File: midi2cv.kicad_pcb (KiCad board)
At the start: 2 copper layers, 20.2 x 123.5 mm, 23 parts, among them J1 AudioJack3, J2 Conn_02x05_Top_Bottom, J3 AudioJack2_SwitchT, J4 AudioJack2_SwitchT, J5 AudioJack2_SwitchT, J6 AudioJack2_SwitchT, J7 AudioJack3, Q1 BC548, U1 6N138

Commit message: routed pcb
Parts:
- removed Q1: BC548, Package_TO_SOT_THT:TO-92_Inline_Wide
- added B2: Board, Custom:Board_4hp_100mm, F.Cu at (127.0, 95.2)
- added B3: Front_Plate, Custom:Front_Plate_4hp_cut, F.Cu at (190.5, 95.2)
- added C10: 1n, Capacitor_SMD:C_0603_1608Metric, F.Cu at (121.5, 141.5)
- added C11: 1n, Capacitor_SMD:C_0603_1608Metric, F.Cu at (135.3, 141.5)
- added C12: 1n, Capacitor_SMD:C_0603_1608Metric, F.Cu at (132.3, 141.0)
- added C13: 1n, Capacitor_SMD:C_0603_1608Metric, F.Cu at (121.5, 121.0)
- added C14: 1n, Capacitor_SMD:C_0603_1608Metric, F.Cu at (123.1, 116.0)
- added C17: 10n, Capacitor_SMD:C_0603_1608Metric, F.Cu at (128.8, 123.4)
- added C7: 1n, Capacitor_SMD:C_0603_1608Metric, F.Cu at (118.9, 140.7)
- added C8: 100n, Capacitor_SMD:C_0603_1608Metric, F.Cu at (128.8, 135.6)
- added C9: 100n, Capacitor_SMD:C_0603_1608Metric, F.Cu at (125.1, 142.7)
- added D2: 1N5819WS, Diode_SMD:D_SOD-323, F.Cu at (120.1, 78.7)
- added D3: 1N5819WS, Diode_SMD:D_SOD-323, F.Cu at (131.8, 78.7)
- added D5: LED, LED_THT:LED_D3.0mm, B.Cu at (121.9, 94.0)
- added D6: LED, LED_THT:LED_D3.0mm, B.Cu at (129.5, 94.0)
- added H1: 6mm, Custom:DrillHole_D6.00, F.Cu at (185.4, 52.1)
- added H10: 7mm, Custom:DrillHole_D7.00, F.Cu at (190.5, 112.4)
- added H2: 6mm, Custom:DrillHole_D6.00, F.Cu at (185.4, 63.5)
- added H3: 6mm, Custom:DrillHole_D6.00, F.Cu at (190.5, 126.4)
- added H4: 6mm, Custom:DrillHole_D6.00, F.Cu at (185.4, 138.4)
- added H5: 6mm, Custom:DrillHole_D6.00, F.Cu at (195.6, 52.1)
- added H6: 6mm, Custom:DrillHole_D6.00, F.Cu at (195.6, 63.5)
- added H7: 6mm, Custom:DrillHole_D6.00, F.Cu at (195.6, 138.4)
- added H8: 3mm, Custom:DrillHole_D3.00, F.Cu at (186.7, 94.0)
- added H9: 3mm, Custom:DrillHole_D3.00, F.Cu at (194.3, 94.0)
- added J8: CC, Custom:Jack_3.5mm_QingPu_WQP-PJ398SM_Vertical_CircularHoles_L, B.Cu at (127.0, 126.4)
- added J9: Conn_02x04_Odd_Even, Connector_PinSocket_1.27mm:PinSocket_2x04_P1.27mm_Vertical, F.Cu at (119.4, 131.4)
- added JP1: Jumper_3_Bridged12, Connector_PinHeader_2.54mm:PinHeader_1x03_P2.54mm_Vertical, F.Cu at (134.6, 126.9)
- added R10: 1k, Resistor_SMD:R_0603_1608Metric, F.Cu at (129.3, 143.3)
- added R11: 1k, Resistor_SMD:R_0603_1608Metric, F.Cu at (132.1, 97.2)
- added R12: 15k, Resistor_SMD:R_0603_1608Metric, F.Cu at (118.9, 137.4)
- added R13: 15k, Resistor_SMD:R_0603_1608Metric, F.Cu at (121.5, 140.0)
- added R14: 15k, Resistor_SMD:R_0603_1608Metric, F.Cu at (135.3, 138.4)
- added R15: 15k, Resistor_SMD:R_0603_1608Metric, F.Cu at (132.3, 139.3)
- added R16: 15k, Resistor_SMD:R_0603_1608Metric, F.Cu at (121.5, 116.0)
- added R17: 15k, Resistor_SMD:R_0603_1608Metric, F.Cu at (122.3, 118.2)
- added R18: 100, Resistor_SMD:R_0603_1608Metric, F.Cu at (131.4, 120.7)
- added R23: 1k, Resistor_SMD:R_0603_1608Metric, F.Cu at (125.5, 123.4)
- added R24: 1k, Resistor_SMD:R_0603_1608Metric, F.Cu at (119.8, 67.3)
- added R25: 100k, Resistor_SMD:R_0603_1608Metric, F.Cu at (130.8, 130.3)
- added R27: 1k, Resistor_SMD:R_0603_1608Metric, F.Cu at (128.9, 96.5)
- added R7: 1k, Resistor_SMD:R_0603_1608Metric, F.Cu at (122.4, 137.7)
- added R8: 1k, Resistor_SMD:R_0603_1608Metric, F.Cu at (124.9, 67.3)
- added R9: 1k, Resistor_SMD:R_0603_1608Metric, F.Cu at (127.6, 67.3)
- added RV1: 20k, Potentiometer_THT:Potentiometer_Vishay_T93XA_Horizontal, B.Cu at (124.5, 104.8)
- added RV2: 100k, Potentiometer_THT:Potentiometer_Vishay_T93XA_Horizontal, B.Cu at (124.5, 99.1)
- added RV5: A100k, EuroRackTools:Potentiometer_Alpha_RD901F-40-00D_Single_Vertical, B.Cu at (129.5, 120.0)
- added U3: TL072, Package_SO:SOIC-8_3.9x4.9mm_P1.27mm, F.Cu at (127.0, 139.2)
- added U4: TL072, Package_SO:SOIC-8_3.9x4.9mm_P1.27mm, F.Cu at (127.0, 108.6)
- C1: footprint Capacitor_THT:C_Disc_D3.0mm_W2.0mm_P2.50mm -> Capacitor_SMD:C_0603_1608Metric
- C2, C3: value 100p -> 100n; footprint Capacitor_THT:C_Disc_D3.0mm_W2.0mm_P2.50mm -> Capacitor_SMD:C_0603_1608Metric
- C4, C5, C6: footprint Capacitor_THT:CP_Radial_D5.0mm_P2.00mm -> Capacitor_SMD:C_0805_2012Metric
- D1: value 1N4148 -> 1N4148WS; footprint Diode_THT:D_DO-35_SOD27_P2.54mm_Vertical_AnodeUp -> Diode_SMD:D_SOD-323
- J1: value AudioJack3 -> MIDI In; footprint TRS_AudioConn3:Jack_3.5mm_QingPu_WQP-PJ366ST_Vertical -> Custom:Jack_3.5mm_QingPu_WQP-PJ366ST_Vertical_CircularHoles_L; moved to B.Cu
- J2: value Conn_02x05_Top_Bottom -> EuroPower10_THT; footprint Connector_IDC:IDC-Header_2x05_P2.54mm_Vertical -> Custom:IDC-Header_2x05_P2.54mm_Vertical_PinOnly
- J3: value AudioJack2_SwitchT -> Pitch; footprint Connector_Audio:Jack_3.5mm_QingPu_WQP-PJ398SM_Vertical_CircularHoles -> Custom:Jack_3.5mm_QingPu_WQP-PJ398SM_Vertical_CircularHoles_R; moved to B.Cu
- J4: value AudioJack2_SwitchT -> Clock; footprint Connector_Audio:Jack_3.5mm_QingPu_WQP-PJ398SM_Vertical_CircularHoles -> Custom:Jack_3.5mm_QingPu_WQP-PJ398SM_Vertical_CircularHoles_L; moved to B.Cu
- J5: value AudioJack2_SwitchT -> Clock2; footprint Connector_Audio:Jack_3.5mm_QingPu_WQP-PJ398SM_Vertical_CircularHoles -> Custom:Jack_3.5mm_QingPu_WQP-PJ398SM_Vertical_CircularHoles_L; moved to B.Cu
- J6: value AudioJack2_SwitchT -> Gate; footprint Connector_Audio:Jack_3.5mm_QingPu_WQP-PJ398SM_Vertical_CircularHoles -> Custom:Jack_3.5mm_QingPu_WQP-PJ398SM_Vertical_CircularHoles_L; moved to B.Cu
- J7: value AudioJack3 -> MIDI Through; footprint TRS_AudioConn3:Jack_3.5mm_QingPu_WQP-PJ366ST_Vertical -> Custom:Jack_3.5mm_QingPu_WQP-PJ366ST_Vertical_CircularHoles_L; moved to B.Cu
- R1, R5, R6: footprint Resistor_THT:R_Axial_DIN0207_L6.3mm_D2.5mm_P2.54mm_Vertical -> Resistor_SMD:R_0603_1608Metric
- R2: value 1k -> 10k; footprint Resistor_THT:R_Axial_DIN0207_L6.3mm_D2.5mm_P2.54mm_Vertical -> Resistor_SMD:R_0603_1608Metric
- R3: value 1k -> 1M; footprint Resistor_THT:R_Axial_DIN0207_L6.3mm_D2.5mm_P2.54mm_Vertical -> Resistor_SMD:R_0603_1608Metric
- R4: value 1k -> 100k; footprint Resistor_THT:R_Axial_DIN0207_L6.3mm_D2.5mm_P2.54mm_Vertical -> Resistor_SMD:R_0603_1608Metric
- U1: value 6N138 -> 6N137; footprint Package_DIP:DIP-8_W7.62mm_Socket_LongPads -> Package_SO:SOP-8_6.605x9.655mm_P2.54mm
- moved D1 112.9 mm to (131.4, 52.7), turned to 180 degrees
- moved R6 104.8 mm to (122.6, 50.2)
- moved C5 104.4 mm to (134.6, 79.5), turned to 90 degrees
- moved R1 102.1 mm to (131.4, 50.2)
- moved R5 101.2 mm to (124.7, 55.5), turned to 180 degrees
- moved C6 99.7 mm to (128.0, 78.7), turned to 180 degrees
- moved R4 95.1 mm to (130.8, 128.8)
- moved C4 92.8 mm to (124.0, 78.7)
- moved J6 92.1 mm to (121.9, 138.4), turned to 180 degrees
- moved R2 90.8 mm to (128.0, 80.5)
- moved C1 88.3 mm to (131.8, 80.5)
- moved C2 87.6 mm to (131.4, 106.0), turned to 90 degrees
- moved R3 87.0 mm to (125.7, 101.6), turned to 90 degrees
- moved J1 85.7 mm to (132.1, 52.1)
- moved J7 85.7 mm to (121.9, 52.1)
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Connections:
- A1 pad 1: unconnected-(A1-D1/TX-Pad1) -> CLOCK
- A1 pad 12: unconnected-(A1-D9-Pad12) -> PITCH
- A1 pad 13: unconnected-(A1-D10-Pad13) -> CC
- A1 pad 14: unconnected-(A1-D11-Pad14) -> EXP5
- A1 pad 2: unconnected-(A1-D0/RX-Pad2) -> CLOCK2
- A1 pad 21: unconnected-(A1-A2-Pad21) -> MIDI_IN
- A1 pad 26: unconnected-(A1-A7-Pad26) -> GATE
- A1 pad 29: unconnected-(A1-GND-Pad29) -> B_GND
- A1 pad 6: unconnected-(A1-D3-Pad6) -> EXP1
- A1 pad 8: unconnected-(A1-D5-Pad8) -> EXP3
- A1 pad 9: unconnected-(A1-D6-Pad9) -> EXP7
- C2 pad 1: Net-(C2-Pad1) -> B_+12V
- C3 pad 2: Net-(C3-Pad2) -> B_-12V
- J1 pad S: C_GND -> B_GND
- J2 pad 1: B_-12V -> -12V
- J2 pad 10: B_+12V -> +12V
- J2 pad 2: B_-12V -> -12V
- J2 pad 9: B_+12V -> +12V
- J3 pad S: unconnected-(J3-PadS) -> B_GND
- J3 pad T: unconnected-(J3-PadT) -> Net-(J3-PadT)
- J4 pad S: unconnected-(J4-PadS) -> B_GND
- J4 pad T: unconnected-(J4-PadT) -> Net-(J4-PadT)
- J5 pad S: unconnected-(J5-PadS) -> B_GND
- J5 pad T: unconnected-(J5-PadT) -> Net-(J5-PadT)
- J6 pad S: unconnected-(J6-PadS) -> B_GND
- J6 pad T: unconnected-(J6-PadT) -> Net-(J6-PadT)
- J7 pad R: Net-(C2-Pad1) -> Net-(J7-PadR)
- J7 pad S: C_GND -> B_GND
- J7 pad T: Net-(C3-Pad2) -> Net-(J7-PadT)
- R3 pad 1: B_GND -> Net-(U3A--)
- R3 pad 2: Net-(U1-GND) -> Net-(R3-Pad2)
- R4 pad 2: MIDI_OUT -> Net-(JP1-C)
- R5 pad 2: Net-(C2-Pad1) -> Net-(J7-PadR)
- R6 pad 2: Net-(C3-Pad2) -> Net-(J7-PadT)
- U1 pad 5: Net-(U1-GND) -> B_GND
- U1 pad 7: Net-(U1-GND) -> unconnected-(U1-EN-Pad7)
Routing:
- net B_+12V: track 0.00 -> 110.9 mm, vias 0 -> 2
- net B_+5V: track 0.00 -> 109.7 mm, vias 0 -> 2
- net B_-12V: track 0.00 -> 87.5 mm, vias 0 -> 4
- net Net-(U4B--): track 0.00 -> 65.2 mm, vias 0 -> 2
- net Net-(J6-PadT): track 0.00 -> 52.2 mm, vias 0 -> 1
- net Net-(U3A--): track 0.00 -> 49.1 mm, vias 0 -> 2
- net Net-(D1-K): track 0.00 -> 47.8 mm, vias 0 -> 2
- net Net-(R10-Pad2): track 0.00 -> 45.6 mm, vias 0 -> 1
- net Net-(D1-A): track 0.00 -> 42.0 mm
- net MIDI_IN: track 0.00 -> 39.0 mm, vias 0 -> 1
- net Net-(R25-Pad1): track 0.00 -> 35.9 mm, vias 0 -> 1
- net EXP7: track 0.00 -> 35.9 mm, vias 0 -> 3
- net EXP1: track 0.00 -> 35.6 mm
- net CLOCK2: track 0.00 -> 34.8 mm, vias 0 -> 1
- net B_GND: track 0.00 -> 33.0 mm, vias 0 -> 17
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- added copper zone on B.Cu, net (none)
- added copper zone on F.Cu, net (none)
- added copper zone on B.Cu, net B_GND
- added copper zone on F.Cu, net B_GND
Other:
- board size 20.2 x 123.5 mm -> 20.3 x 128.5 mm
- board text added: "CC"
- board text added: "clock"
- board text added: "gate"
- board text added: "glide"
- board text added: "in"
- board text added: "midi"
- board text added: "pitch"
- board text added: "red"
- board text added: "sync"
- board text added: "thru"
- board text added: "uni"

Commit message: update routing
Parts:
- R24, R27: value 1k -> 4k7
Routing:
- net B_GND: track 33.0 -> 27.1 mm, vias 17 -> 16
- net Net-(D6-K): track 5.51 -> 2.62 mm, vias 1 -> 0
- net MIDI_IN: track 39.0 -> 37.0 mm
- net B_+12V: track 110.9 -> 109.7 mm, vias 2 -> 3
- net SLEW_IN: track 22.9 -> 21.7 mm

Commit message: add gerbers and bom
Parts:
- added B: Board, PCM_kikit:Board, F.Cu at (117.5, 47.6)
- added F: Board, PCM_kikit:Board, F.Cu at (180.3, 34.3)
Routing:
- net CLOCK: track 20.8 -> 19.2 mm

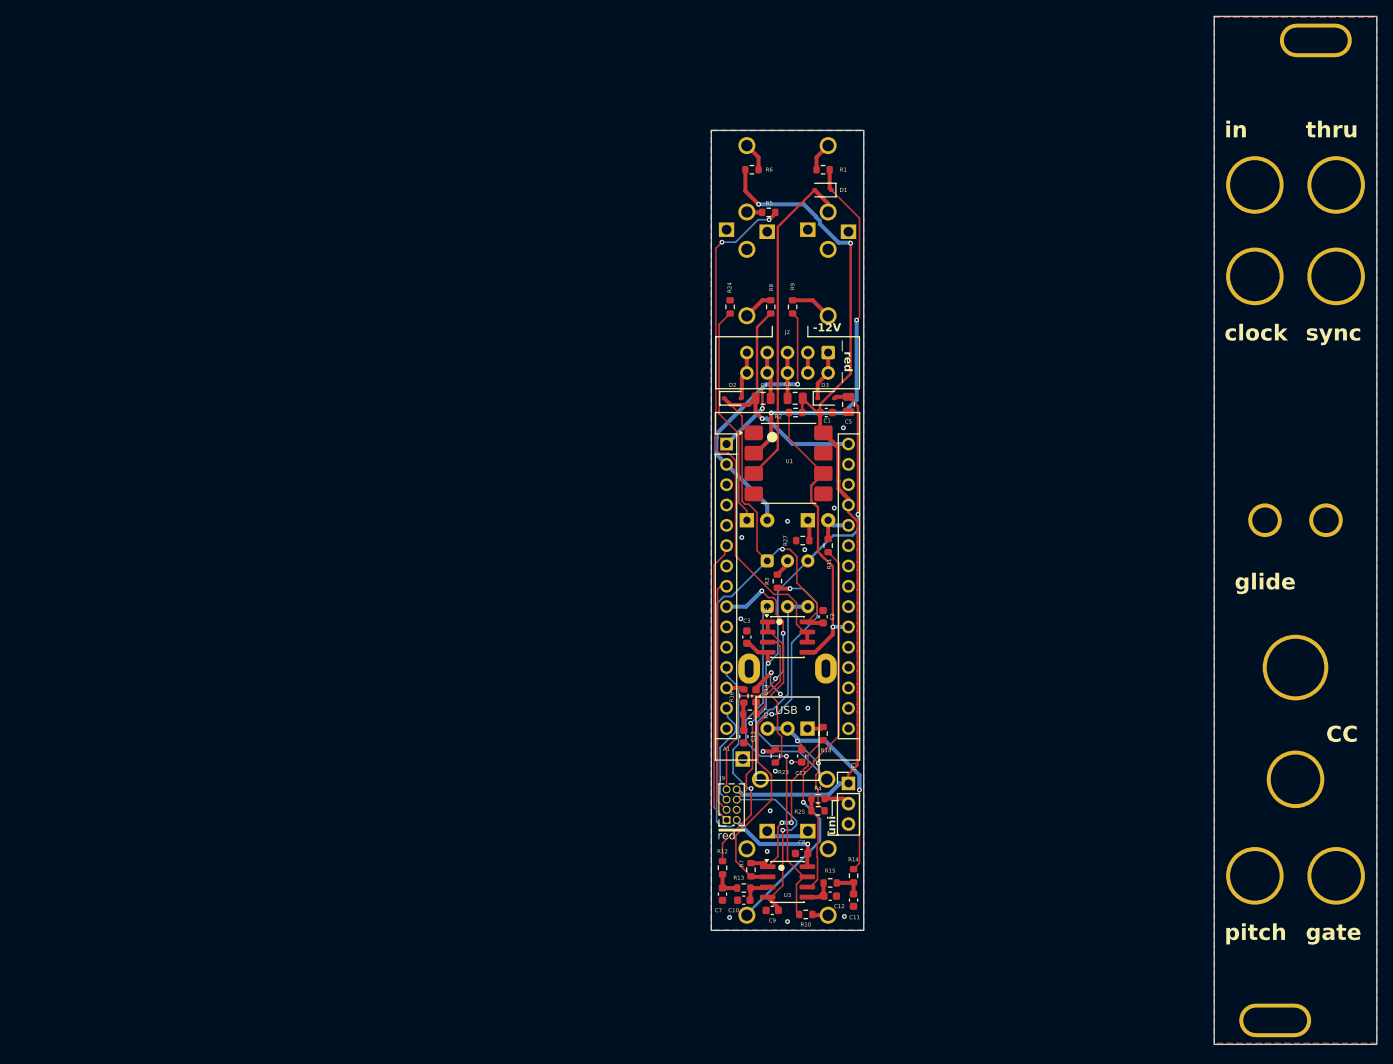
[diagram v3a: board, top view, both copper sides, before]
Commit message: add rev 2 and rev 3, now with correct trs midi A
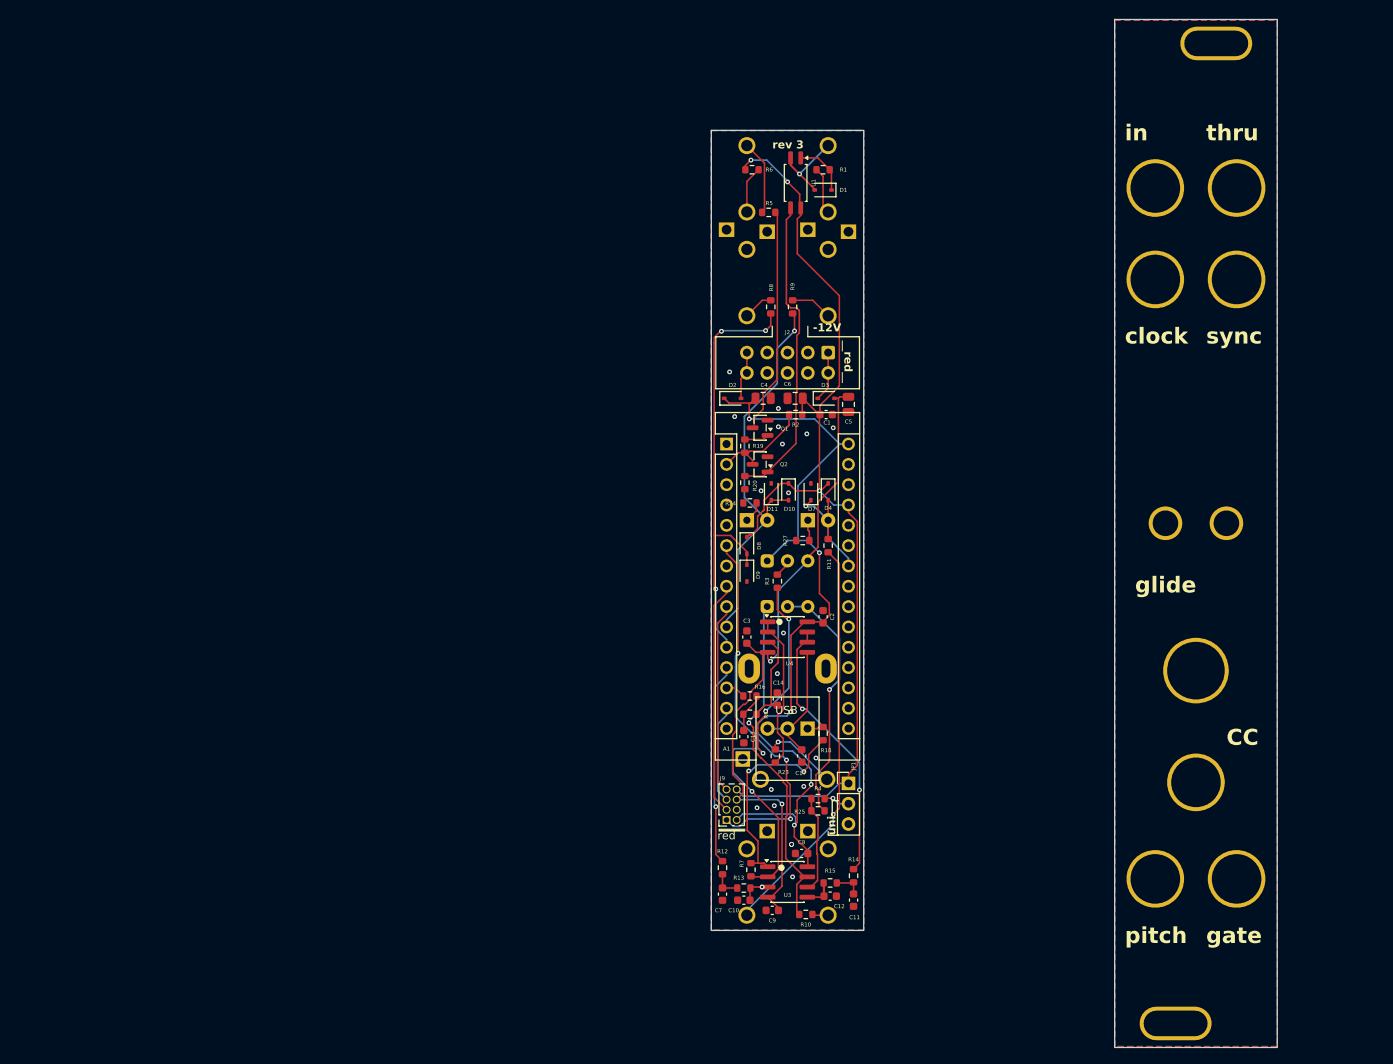
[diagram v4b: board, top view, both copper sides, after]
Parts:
- added D10: 1N5819WS, Diode_SMD:D_SOD-323, F.Cu at (127.1, 90.4)
- added D11: 1N5819WS, Diode_SMD:D_SOD-323, F.Cu at (125.0, 90.4)
- added D4: 1N5819WS, Diode_SMD:D_SOD-323, F.Cu at (132.1, 90.4)
- added D7: 1N5819WS, Diode_SMD:D_SOD-323, F.Cu at (129.9, 90.4)
- added D8: 1N5819WS, Diode_SMD:D_SOD-323, F.Cu at (121.9, 97.2)
- added D9: 1N5819WS, Diode_SMD:D_SOD-323, F.Cu at (121.9, 100.6)
- added Q1: MMBT5551L, Package_TO_SOT_SMD:SOT-23, F.Cu at (123.6, 82.4)
- added Q2: MMBT5551L, Package_TO_SOT_SMD:SOT-23, F.Cu at (123.6, 87.0)
- added R19: 1k, Resistor_SMD:R_0603_1608Metric, F.Cu at (121.7, 84.7)
- added R20: 1k, Resistor_SMD:R_0603_1608Metric, F.Cu at (121.7, 89.3)
- R2: value 10k -> 1k
- U1: value 6N137 -> EL3H7(C)(TA)-G; footprint Package_SO:SOP-8_6.605x9.655mm_P2.54mm -> Package_SO:SSOP-4_4.4x2.6mm_P1.27mm
- moved U1 35.1 mm to (128.0, 51.8), turned to -90 degrees
- moved R24 24.6 mm to (122.3, 91.8), turned to 180 degrees
- moved H5 12.5 mm to (183.1, 52.5)
- moved H6 12.5 mm to (183.1, 63.9)
- moved H7 12.5 mm to (183.1, 138.8)
- moved B3 12.5 mm to (178.1, 95.6)
- moved F 12.5 mm to (167.9, 34.7)
- moved H1 12.5 mm to (173.0, 52.5)
- moved H10 12.5 mm to (178.1, 112.8)
- moved H2 12.5 mm to (173.0, 63.9)
- moved H3 12.5 mm to (178.1, 126.7)
- moved H4 12.5 mm to (173.0, 138.8)
- moved H8 12.5 mm to (174.2, 94.4)
- moved H9 12.5 mm to (181.9, 94.4)
- moved C14 2.69 mm to (125.7, 116.3)
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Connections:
- A1 pad 1: CLOCK -> unconnected-(A1-D1/TX-Pad1)
- A1 pad 10: unconnected-(A1-D7-Pad10) -> CLOCK2
- A1 pad 11: unconnected-(A1-D8-Pad11) -> CLOCK
- A1 pad 2: CLOCK2 -> MIDI_IN
- A1 pad 21: MIDI_IN -> unconnected-(A1-A2-Pad21)
- A1 pad 24: unconnected-(A1-A5-Pad24) -> GATE
- A1 pad 26: GATE -> unconnected-(A1-A7-Pad26)
- C17 pad 1: SLEW_OUT -> Net-(U4B-+)
- J1 pad R: Net-(D1-A) -> Net-(J1-PadR)
- J1 pad S: B_GND -> unconnected-(J1-PadS)
- J1 pad T: Net-(J1-PadT) -> Net-(D1-A)
- R1 pad 1: Net-(J1-PadT) -> Net-(J1-PadR)
- R5 pad 1: Net-(U4B--) -> Net-(Q1-C)
- R5 pad 2: Net-(J7-PadR) -> Net-(J7-PadT)
- R6 pad 2: Net-(J7-PadT) -> Net-(J7-PadR)
- RV5 pad 2: SLEW_OUT -> Net-(U4B-+)
- RV5 pad 3: SLEW_OUT -> Net-(U4B-+)
- U1 pad 1: unconnected-(U1-NC-Pad1) -> Net-(D1-K)
- U1 pad 2: Net-(D1-K) -> Net-(D1-A)
- U1 pad 3: Net-(D1-A) -> Net-(Q2-B)
- U1 pad 4: unconnected-(U1-NC-Pad4) -> B_+5V
- U4 pad 5: MIDI_IN -> Net-(U4B-+)
- U4 pad 6: Net-(U4B--) -> SLEW_OUT
- U4 pad 7: Net-(U4B--) -> SLEW_OUT
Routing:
- net Net-(U4B--): track 65.2 -> 0.00 mm, vias 2 -> 0
- net Net-(D1-K): track 47.9 -> 6.86 mm, vias 2 -> 0
- net Net-(Q2-B): track 0.00 -> 39.0 mm
- net CLOCK: track 19.2 -> 55.1 mm, vias 1 -> 3
- net Net-(D1-A): track 42.0 -> 11.9 mm, vias 0 -> 1
- net Net-(Q1-C): track 0.00 -> 28.3 mm
- net B_GND: track 27.2 -> 0.00 mm, vias 16 -> 19
- net Net-(D5-K): track 27.9 -> 2.66 mm
- net MIDI_IN: track 37.4 -> 13.0 mm, vias 1 -> 0
- net Net-(U4B-+): track 0.00 -> 16.6 mm
- net B_+5V: track 110.0 -> 125.4 mm, vias 2 -> 3
- net CLOCK2: track 35.3 -> 50.0 mm
- net EXP7: track 35.9 -> 23.8 mm, vias 3 -> 0
- net EXP1: track 35.6 -> 47.1 mm, vias 0 -> 3
- net GATE: track 5.15 -> 16.1 mm, vias 0 -> 1
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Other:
- board text added: "rev 3"
